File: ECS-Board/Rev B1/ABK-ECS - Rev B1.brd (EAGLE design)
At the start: 100 x 100 mm, 272 parts, among them J1 USB-B-S-RA, J10 FTSH-105-01-L-DV-NOPASTE, J11 22-05-7028-02, J12 RB1-125BAG1A, J2 MSTBA2, J3 22-05-7068-06, J4 22-05-7028-02, J5 22-05-7068-06, J6 22-05-7068-06, J7 22-05-7068-06, J8 22-05-7028-02, J9 FTSH-103-01-L-DV-NOPASTE, K1 G6K-2G-Y, SW1 B3FS-1015, SW2 B3FS-1015, T1 MMBT2907ALT3, T10 MMBT2222AL, T11 IRLML5103TRPBF, T12 MMBT2222AL, T13 IRLML5103TRPBF, T14 IRLML5103TRPBF, T15 IRLML5103TRPBF, T16 IRLML5103TRPBF, T17 MMBT2222AL, T18 MMBT2222AL, T19 MMBT2222AL, T2 EXMACHINA-LOGO-NAME, T20 MMBT2222AL, T3 IRLML5103TRPBF, T4 IRLML5103TRPBF, T5 IRLML5103TRPBF, T6 IRLML5103TRPBF, T7 MMBT2222AL, T8 MMBT2222AL, T9 MMBT2222AL, U1 AT24C512C-SSHM-B, U2 LPC1768FBD100, U3 LT3686HDDPBF, U4 LT3686HDDPBF, U5 CD4050BD, U6 CD4050BD, U7 DP83848JSQ/NOPB, X1 FC-135, X2 ASE-12, X3 3000, X4 ASE_50

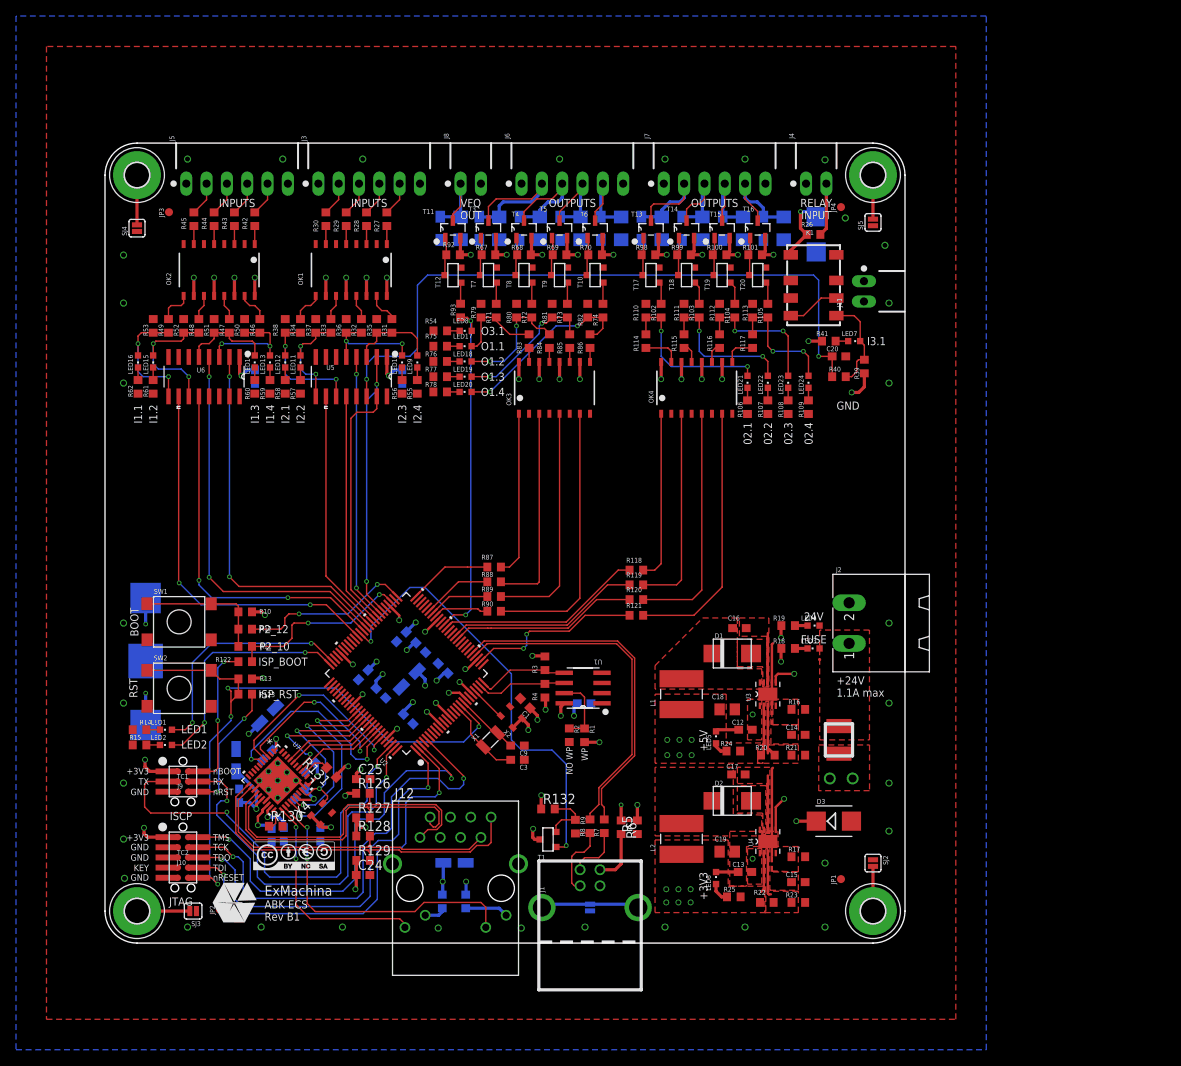
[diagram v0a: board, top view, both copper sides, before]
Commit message: dd pull up and pull down resistor to I2C and UART and place every compoment
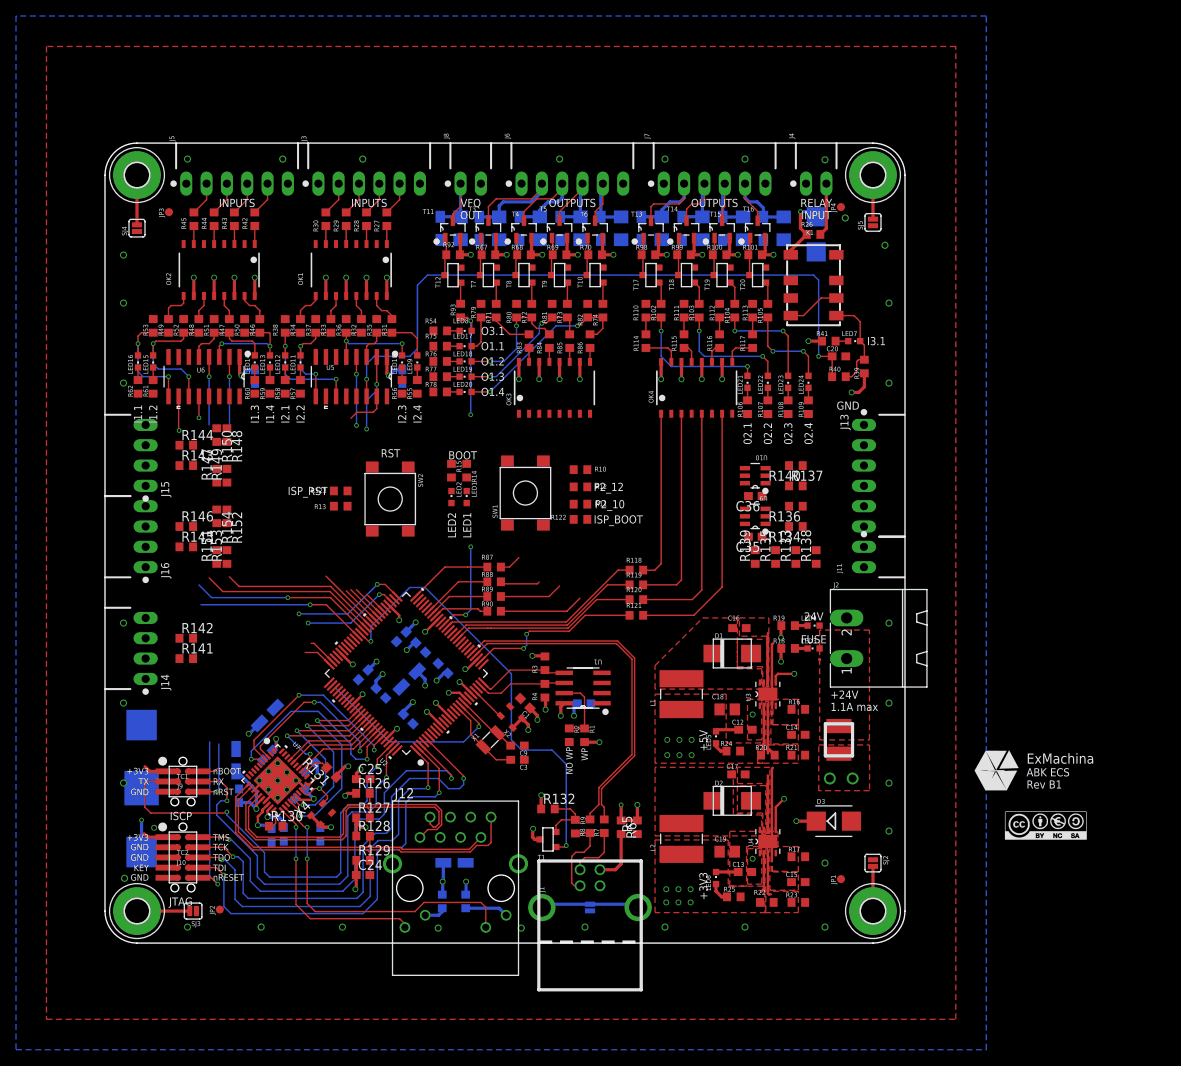
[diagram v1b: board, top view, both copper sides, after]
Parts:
- added C35, C36: 0.1uF, rcl:C0603
- added J13: 22-05-7068-06, con-molex:7395-06
- added J14, J15, J16: 22-05-7048-04, con-molex:7395-04
- added R133, R135, R138, R139: 4K7, rcl:R0603
- added R134, R136, R137, R140, R141, R142, R143, R144, R145, R146, R147, R148, R149, R150, R151, R152, R153, R154: 1K, rcl:R0603
- added U10, U9: SN74LVC2G17DBVR, ti:SOT95P280X145-6N
- moved T2 96.7 mm to (111.4, 21.5)
- moved CC1 94.1 mm to (117.6, 14.7)
- moved R14 52.2 mm to (45.2, 59.1), turned to 90 degrees
- moved R15 51.9 mm to (43.3, 59.1), turned to 90 degrees
- moved LED1 47.5 mm to (45.2, 55.8), turned to 0 degrees
- moved LED2 47.3 mm to (43.3, 55.8), turned to 0 degrees
- moved SW1 46.2 mm to (52.6, 56.3), turned to 90 degrees
- moved R10 45.5 mm to (59.4, 59.2)
- moved R11 45.5 mm to (59.4, 54.9)
- moved R12 45.5 mm to (59.4, 57.0)
- moved R122 45.5 mm to (59.4, 53.0)
- moved SW2 35.4 mm to (35.7, 55.5), turned to 270 degrees
- moved J11 33.2 mm to (94.9, 48.3)
- moved R123 28.1 mm to (29.5, 56.5), turned to 180 degrees
- moved R13 24.7 mm to (29.5, 54.6), turned to 180 degrees
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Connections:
- new net N$117: J13.5, R133.2, R134.1
- new net N$118: J13.4, R136.1, R138.2
- new net N$119: J13.3, R135.2, R137.1
- new net N$120: R140.2, U10.3
- new net N$121: R136.2, U9.3
- new net N$122: R134.2, U9.1
- new net N$123: R137.2, U10.1
- new net N$124: J13.2, R139.2, R140.1
- new net N$125: J14.2, R141.1
- new net N$126: J14.3, R142.1
- new net N$127: J15.2, R143.1
- new net N$128: J15.3, R144.1
- new net N$129: J16.2, R145.1
- new net N$130: J16.3, R146.1
- net +3V3: now also C35.1, C36.1, J15.1, J16.1, R149.1, R150.1, R153.1, R154.1, U10.5, U9.5
- net +5V: now also J13.6, R133.1, R135.1, R138.1, R139.1
- net ADC1: now also R141.2
- net ADC2: now also R142.2
- net ENCODER_A: now also U9.6
- net ENCODER_B: now also U9.4
- net ENCODER_PUSH: now also U10.4
- net ENCODER_Z: now also U10.6
- net GND: now also C35.2, C36.2, J13.1, J14.4, J15.4, J16.4, R147.1, R148.1, R151.1, R152.1, U10.2, U9.2
- net I2C_SCL: now also R144.2, R148.2, R150.2
- net I2C_SDA: now also R143.2, R147.2, R149.2
- net UART_RX: now also R146.2, R152.2, R154.2
- net UART_TX: now also R145.2, R151.2, R153.2
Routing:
- net VBAT+: track 59.1 -> 6.55 mm, vias 3 -> 2
- net !RESET: track 83.9 -> 47.3 mm, vias 4 -> 2
- net ONBOARD_LED2: track 29.8 -> 3.55 mm, vias 2 -> 0
- net ONBOARD_LED1: track 29.6 -> 3.63 mm, vias 2 -> 0
- net INPUT2.1_MCU: track 29.3 -> 5.00 mm
- net N$43: track 33.6 -> 10.5 mm
- net INPUT1.1_MCU: track 48.4 -> 25.5 mm
- net INPUT2.2_MCU: track 30.6 -> 8.09 mm
- net N$46: track 29.4 -> 7.87 mm
- net INPUT3.1_MCU: track 31.4 -> 9.97 mm
- net N$42: track 26.0 -> 4.99 mm
- net INPUT1.2_MCU: track 46.5 -> 25.6 mm
- net INPUT2.4_MCU: track 33.1 -> 12.4 mm
- net INPUT2.3_MCU: track 33.3 -> 12.8 mm
- net INPUT1.3_MCU: track 49.8 -> 30.7 mm, vias 2 -> 1
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
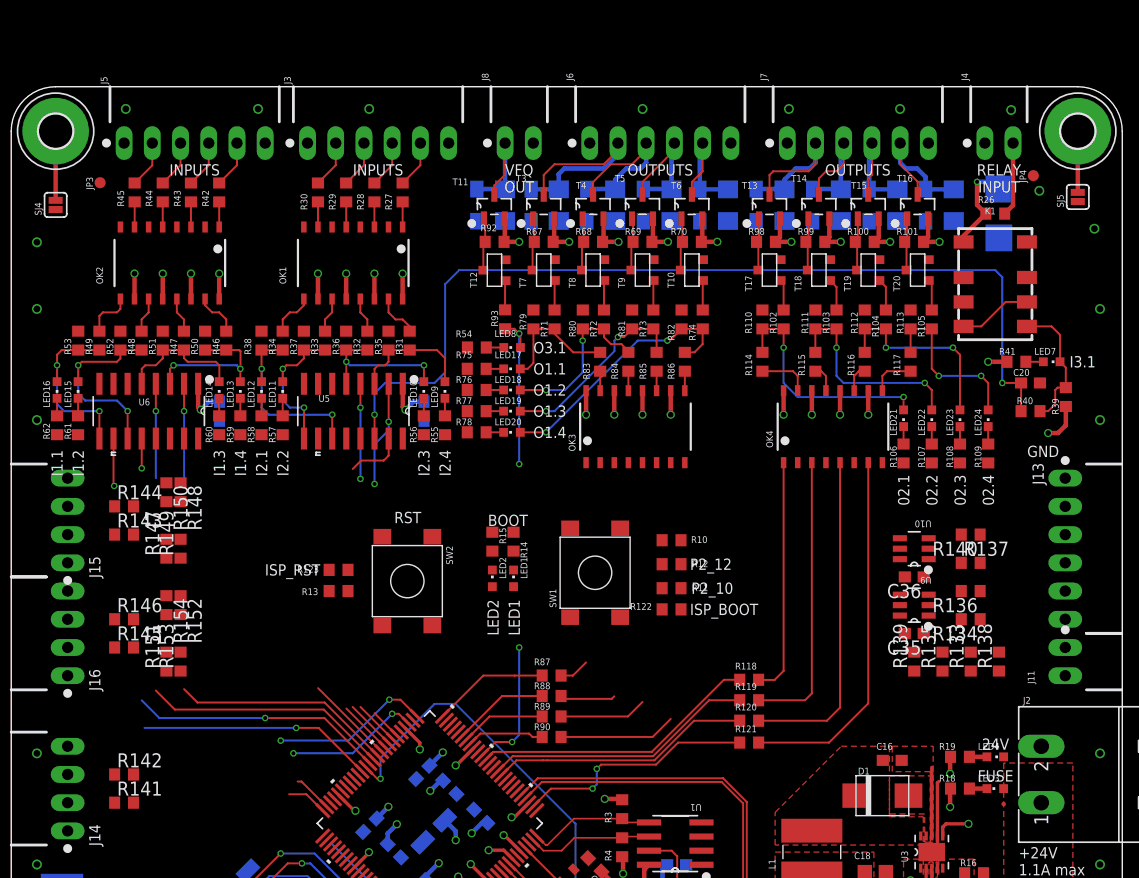
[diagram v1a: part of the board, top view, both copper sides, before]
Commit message: Delete realy input
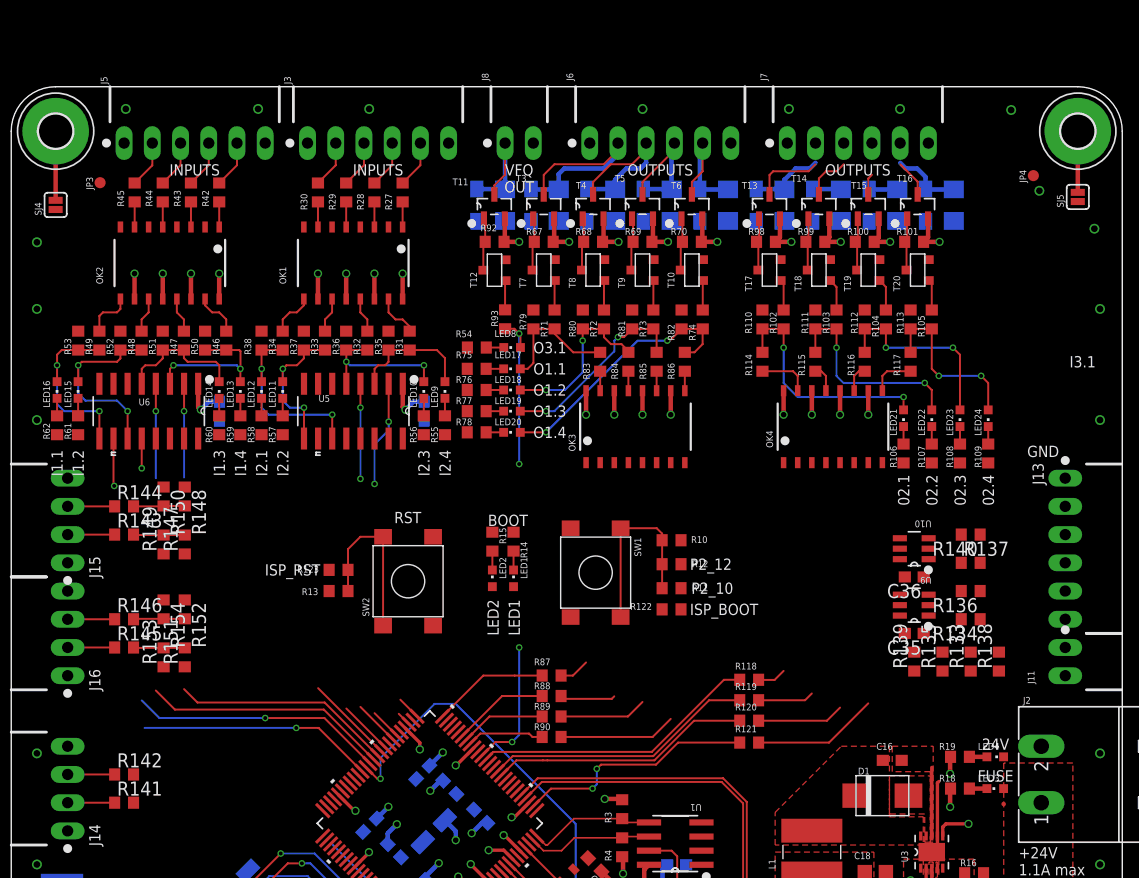
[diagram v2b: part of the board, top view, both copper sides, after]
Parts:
- removed C20: 0.1uF, rcl:C0603
- removed D4: STPS3L40UF, diode:SMB
- removed J4: 22-05-7028-02, con-molex:7395-02
- removed K1: G6K-2G-Y, relay:G6K-2G-Y
- removed LED7: Red, led:CHIPLED_0603
- removed R26, R40: 100, rcl:R0603
- removed R39: 4K7, rcl:R0603
- removed R41: 1K5, rcl:R0603
- moved R147 1.69 mm to (15.6, 58.8)
- moved R151 1.69 mm to (15.6, 48.6)
- moved R149 1.57 mm to (13.7, 58.8)
- moved R153 1.57 mm to (13.7, 48.6)
- moved R148 0.54 mm to (15.6, 63.1)
- moved R152 0.54 mm to (15.6, 53.0)
- moved R150 0.46 mm to (13.7, 63.1)
- moved R154 0.46 mm to (13.7, 53.0)
- moved SW2 0.07 mm to (35.7, 55.5), turned to 90 degrees
- turned SW1 to 270 degrees
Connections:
- removed net INPUT3.1: C20.1, R40.2, U5.14
- removed net INPUT3.1_MCU: U2.58, U5.15
- removed net N$28: D4.C, K1.1, R26.2
- removed net N$32: J4.2, R26.1
- removed net N$60: K1.4, K1.6
- removed net N$73: K1.5, LED7.C, R39.2, R40.1
- removed net N$74: LED7.A, R41.1
- net +24V: no longer J4.1
- net +5V: no longer R39.1, R41.2
- net GND: no longer C20.2, D4.A, K1.3, K1.8
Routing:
- net INPUT3.1: track 83.8 -> 0.00 mm, vias 2 -> 0
- net N$93: track 29.9 -> 7.82 mm
- net N$92: track 33.0 -> 11.3 mm
- net N$91: track 25.8 -> 5.04 mm
- net N$89: track 21.3 -> 2.59 mm
- net N$5: track 0.00 -> 16.9 mm
- net !RESET: track 47.3 -> 62.7 mm
- net N$73: track 12.6 -> 0.00 mm
- net BOOT_SELECT_P2_12: track 14.4 -> 2.12 mm, vias 2 -> 0
- net BOOT_SELECT_P2_10: track 12.3 -> 1.33 mm, vias 2 -> 0
- net INPUT3.1_MCU: track 9.97 -> 0.00 mm
- net N$28: track 8.80 -> 0.00 mm, vias 1 -> 0
- net OUTPUT2.3: track 11.6 -> 4.47 mm
- net N$32: track 6.66 -> 0.00 mm
- net N$60: track 6.61 -> 0.00 mm
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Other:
- board text removed: "RELAY INPUT"

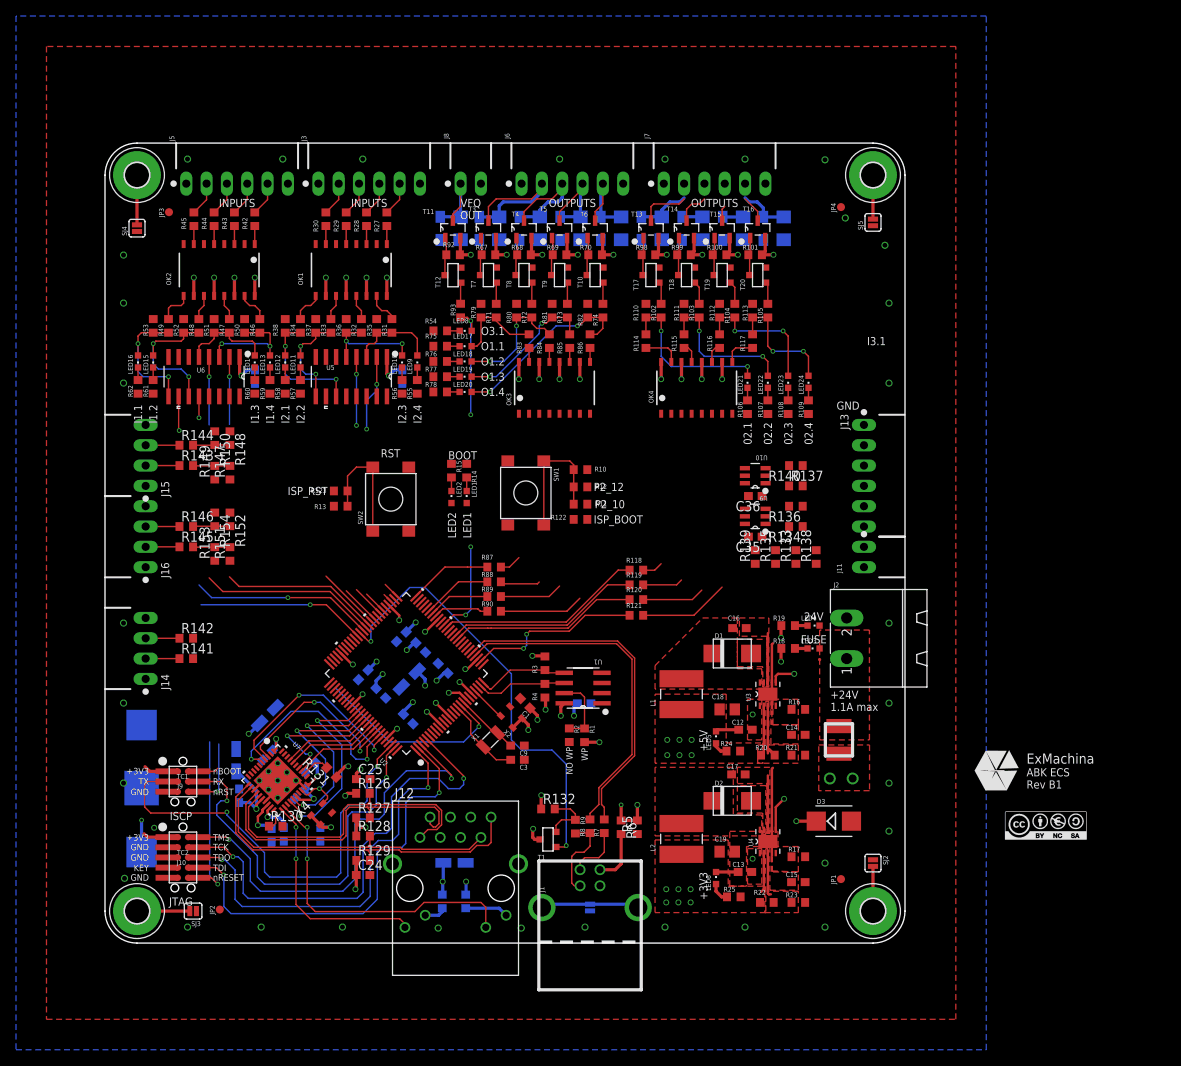
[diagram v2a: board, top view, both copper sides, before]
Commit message: Route USB LED, re-place IO leds
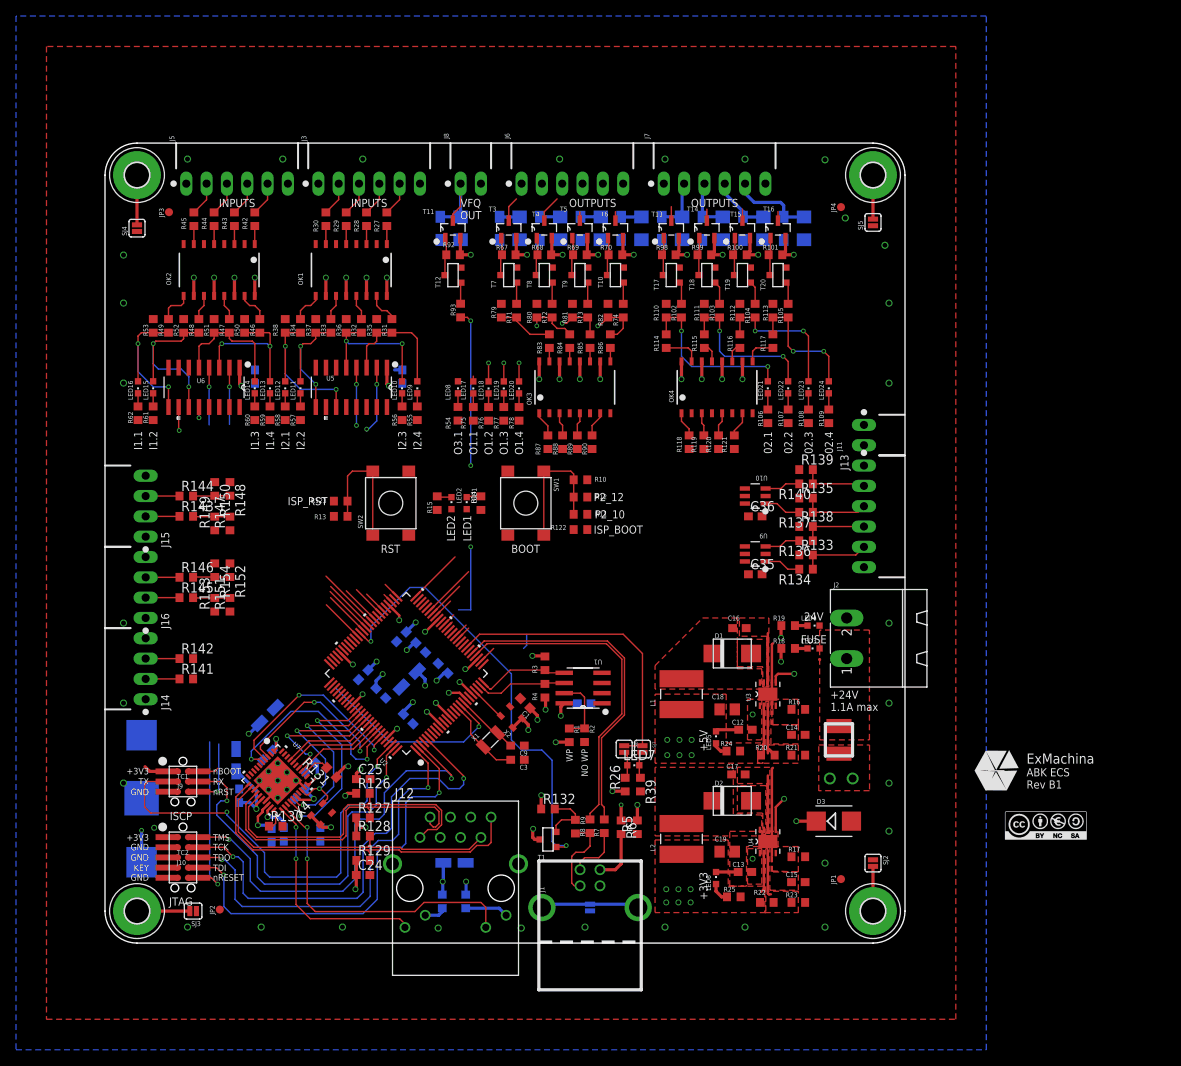
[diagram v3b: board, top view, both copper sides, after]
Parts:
- added LED7: Blue, led:CHIPLED_0603
- added R26, R39: 1K5, rcl:R0603
- added SJ6, SJ7: SJNC, SparkFun-Passives:SJ_2S
- moved R121 24.9 mm to (78.7, 62.6), turned to 270 degrees
- moved R90 24.4 mm to (60.9, 62.6), turned to 270 degrees
- moved R120 22.2 mm to (76.7, 62.6), turned to 270 degrees
- moved R89 21.9 mm to (59.0, 62.6), turned to 270 degrees
- moved R119 19.7 mm to (74.9, 62.6), turned to 270 degrees
- moved R88 19.4 mm to (57.2, 62.6), turned to 270 degrees
- moved R118 17.3 mm to (73.0, 62.6), turned to 270 degrees
- moved R87 17.0 mm to (55.4, 62.6), turned to 270 degrees
- moved J11 15.2 mm to (94.9, 63.5)
- moved R139 12.6 mm to (87.6, 59.2), turned to 0 degrees
- moved R54 10.6 mm to (44.1, 66.2), turned to 270 degrees
- moved R78 10.2 mm to (51.8, 66.2), turned to 270 degrees
- moved R75 9.42 mm to (46.0, 66.2), turned to 270 degrees
- moved R77 9.21 mm to (49.9, 66.2), turned to 270 degrees
- moved R76 8.92 mm to (47.9, 66.2), turned to 270 degrees
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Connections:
- new net N$28: LED7.A, R26.2, SJ6.2
- new net N$32: LED7.C, R39.1, SJ7.2
- net +3V3: now also R26.1
- net GND: now also R39.2
- net USB_LED: now also SJ6.1, SJ7.1
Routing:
- net USB_LED: track 0.00 -> 37.5 mm
- net OUTPUT2.1_MCU: track 25.8 -> 0.98 mm
- net OUTPUT2.2_MCU: track 24.5 -> 1.94 mm
- net OUTPUT2.3_MCU: track 23.5 -> 1.90 mm
- net INPUT1.2_MCU: track 25.6 -> 7.13 mm, vias 2 -> 1
- net OUTPUT2.4_MCU: track 21.8 -> 4.24 mm, vias 2 -> 0
- net INPUT1.3_MCU: track 30.7 -> 13.5 mm
- net INPUT1.1_MCU: track 25.5 -> 8.49 mm, vias 2 -> 1
- net OUTPUT1.1: track 21.0 -> 5.62 mm
- net INPUT1.4_MCU: track 28.3 -> 13.9 mm
- net N$37: track 23.6 -> 9.22 mm
- net OUTPUT1.2: track 16.3 -> 5.93 mm
- net N$36: track 17.8 -> 8.03 mm
- net OUTPUT1.3: track 12.6 -> 3.67 mm
- net N$117: track 0.00 -> 8.59 mm
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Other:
- board text removed: "I3.1"

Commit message: Route Input
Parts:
- moved T2 62.7 mm to (53.0, 44.4)
- moved CC1 53.8 mm to (72.8, 44.4)
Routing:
- net INPUT1.1_MCU: track 8.49 -> 42.0 mm, vias 1 -> 2
- net INPUT1.2_MCU: track 7.13 -> 39.9 mm, vias 1 -> 2
- net INPUT1.3_MCU: track 13.5 -> 44.3 mm, vias 1 -> 2
- net INPUT1.4_MCU: track 13.9 -> 43.7 mm, vias 1 -> 2
- net INPUT2.1_MCU: track 5.00 -> 28.0 mm, vias 0 -> 2
- net INPUT2.2_MCU: track 8.09 -> 29.2 mm, vias 0 -> 2
- net INPUT2.3_MCU: track 11.4 -> 32.0 mm
- net INPUT2.4_MCU: track 11.6 -> 31.7 mm
- net N$37: track 9.22 -> 22.6 mm
- net N$36: track 8.03 -> 19.4 mm
- net N$34: track 8.91 -> 19.1 mm
- net N$31: track 7.79 -> 17.6 mm
- net OUTPUT3.2_MCU: track 30.8 -> 38.9 mm
- net BOOT_SELECT_P2_12: track 2.12 -> 0.00 mm
- net BOOT_SELECT_P2_10: track 1.33 -> 0.00 mm
